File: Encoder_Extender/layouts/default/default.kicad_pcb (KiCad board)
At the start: 2 copper layers, 75 x 30 mm, 15 parts

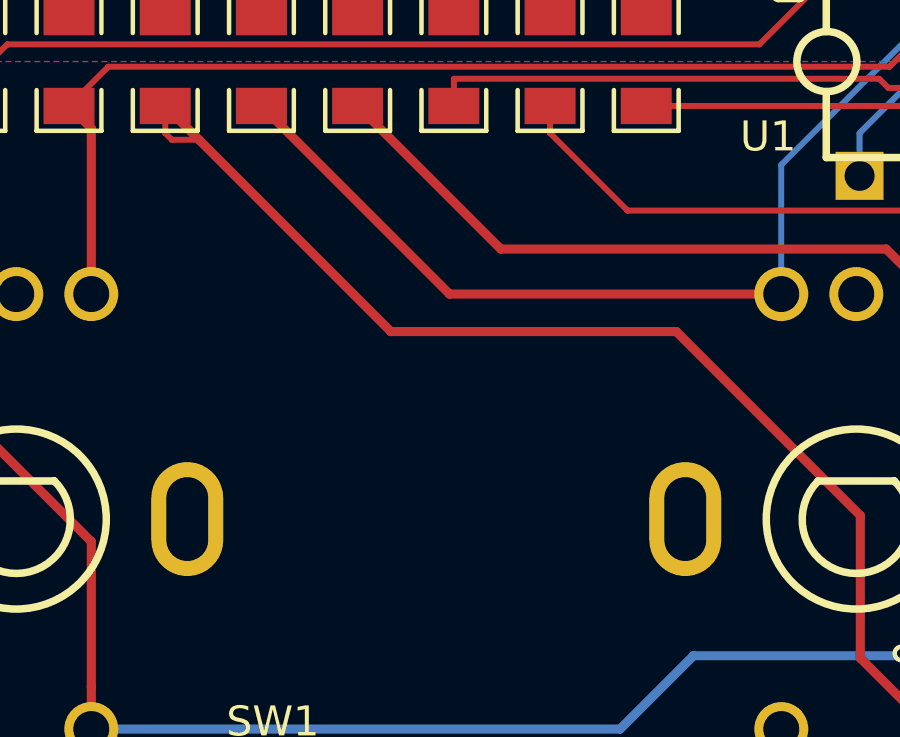
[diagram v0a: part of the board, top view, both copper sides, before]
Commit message: Added silkscreen
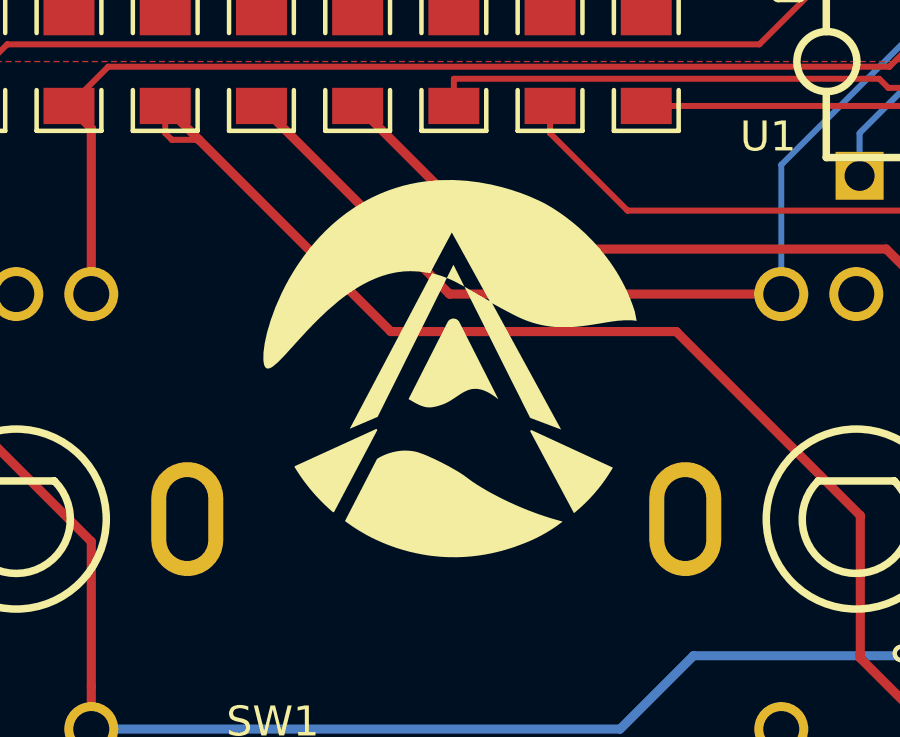
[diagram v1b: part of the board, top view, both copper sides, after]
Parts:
- added QR*****: LED-GitHub-QR-MD, Silkscreen:LED-GitHub-QR-MD, B.Cu at (109.5, 106.2)
- added REF**: OSHW-Logo2_7.3x6mm_SilkScreen, Symbol:OSHW-Logo2_7.3x6mm_SilkScreen, B.Cu at (122.8, 117.8)
- added REF**: KiCad-Logo2_5mm_SilkScreen, Symbol:KiCad-Logo2_5mm_SilkScreen, B.Cu at (122.8, 124.2)
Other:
- board text added: "Rotary Encoder Extender v1.0.0 - June 2026"
